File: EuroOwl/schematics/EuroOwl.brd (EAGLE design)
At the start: 100 x 99.8 mm, 122 parts, among them IC1 QUAD_OPAMPD, IC2 QUAD_OPAMPD, IC3 TL072D, Q900 BC846, Q901 BC846, X1 USBPTH-VERTICAL

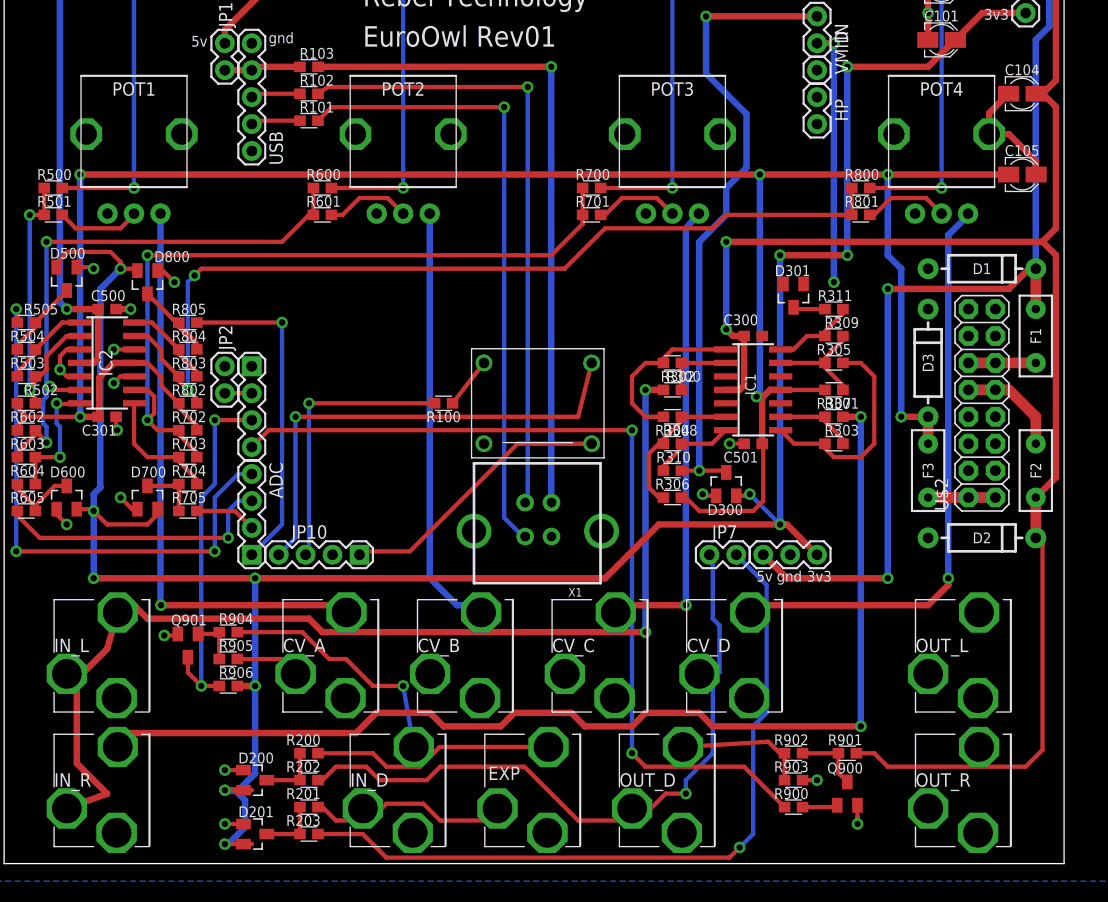
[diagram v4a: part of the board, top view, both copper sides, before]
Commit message: moved USB connector downwards
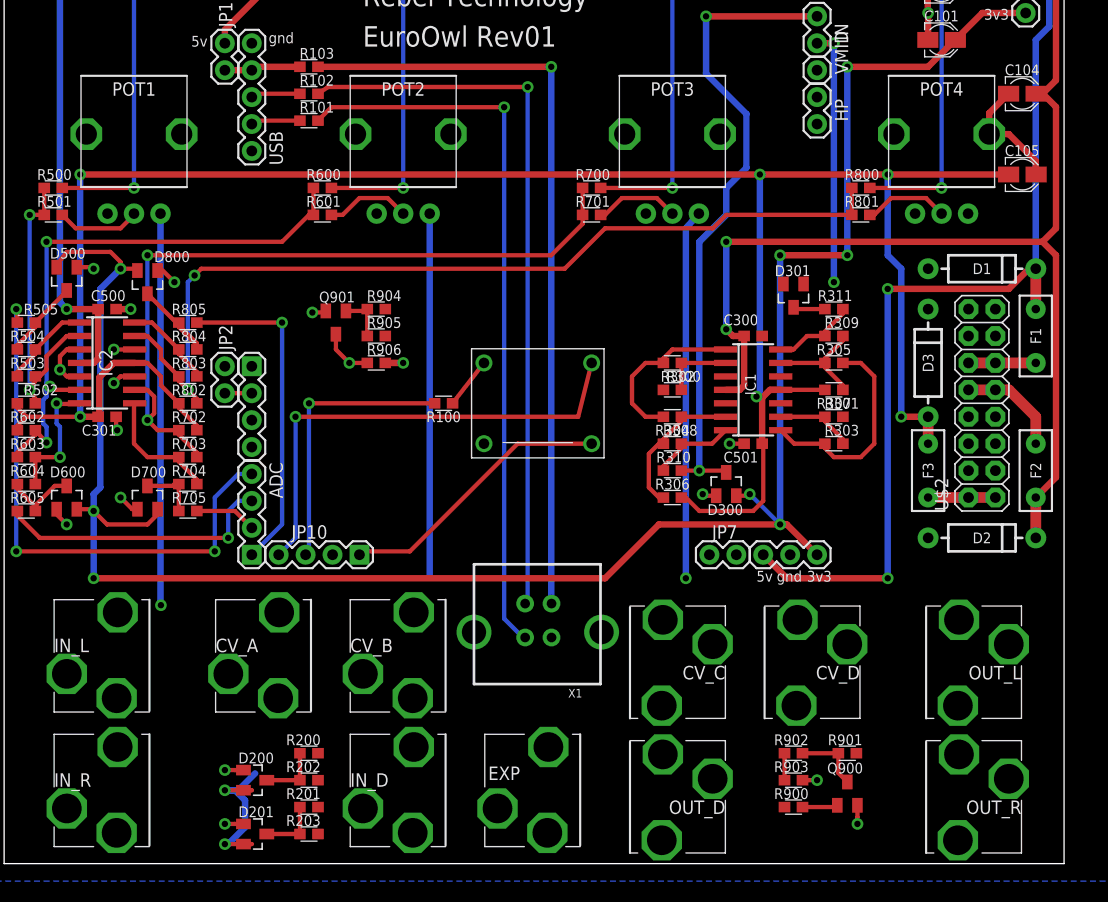
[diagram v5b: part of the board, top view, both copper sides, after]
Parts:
- moved R904 33.5 mm to (35.6, 53.3)
- moved Q901 33.5 mm to (31.8, 52.1)
- moved R905 33.5 mm to (35.6, 50.8)
- moved R906 33.5 mm to (35.6, 48.3)
- moved X1 9.52 mm to (50.8, 22.9)
- moved CV_D 6.35 mm to (76.2, 20.3), turned to 180 degrees
- moved CV_A 6.35 mm to (25.4, 20.3)
- moved CV_B 6.35 mm to (38.1, 20.3)
- moved CV_C 6.35 mm to (63.5, 20.3), turned to 180 degrees
- turned OUT_D to 180 degrees
- turned OUT_L to 180 degrees
- turned OUT_R to 180 degrees
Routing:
- net IN_R: track 106.0 -> 0.00 mm, vias 2 -> 0
- net IN_L: track 99.1 -> 0.00 mm, vias 2 -> 0
- net PB6: track 83.5 -> 0.00 mm, vias 2 -> 0
- net PA3: track 71.0 -> 0.00 mm, vias 1 -> 0
- net PA2: track 63.7 -> 0.00 mm, vias 1 -> 0
- net N$30: track 57.2 -> 0.00 mm, vias 1 -> 0
- net +12V: track 294.3 -> 255.3 mm
- net PB7: track 34.0 -> 4.93 mm, vias 2 -> 1
- net N$46: track 23.6 -> 0.00 mm, vias 1 -> 0
- net N$38: track 23.0 -> 0.00 mm
- net N$47: track 19.3 -> 0.00 mm
- net +3V3: track 231.9 -> 213.5 mm, vias 12 -> 11
- net N$2: track 54.7 -> 37.0 mm
- net N$24: track 45.9 -> 34.9 mm
- net N$49: track 12.6 -> 2.54 mm
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
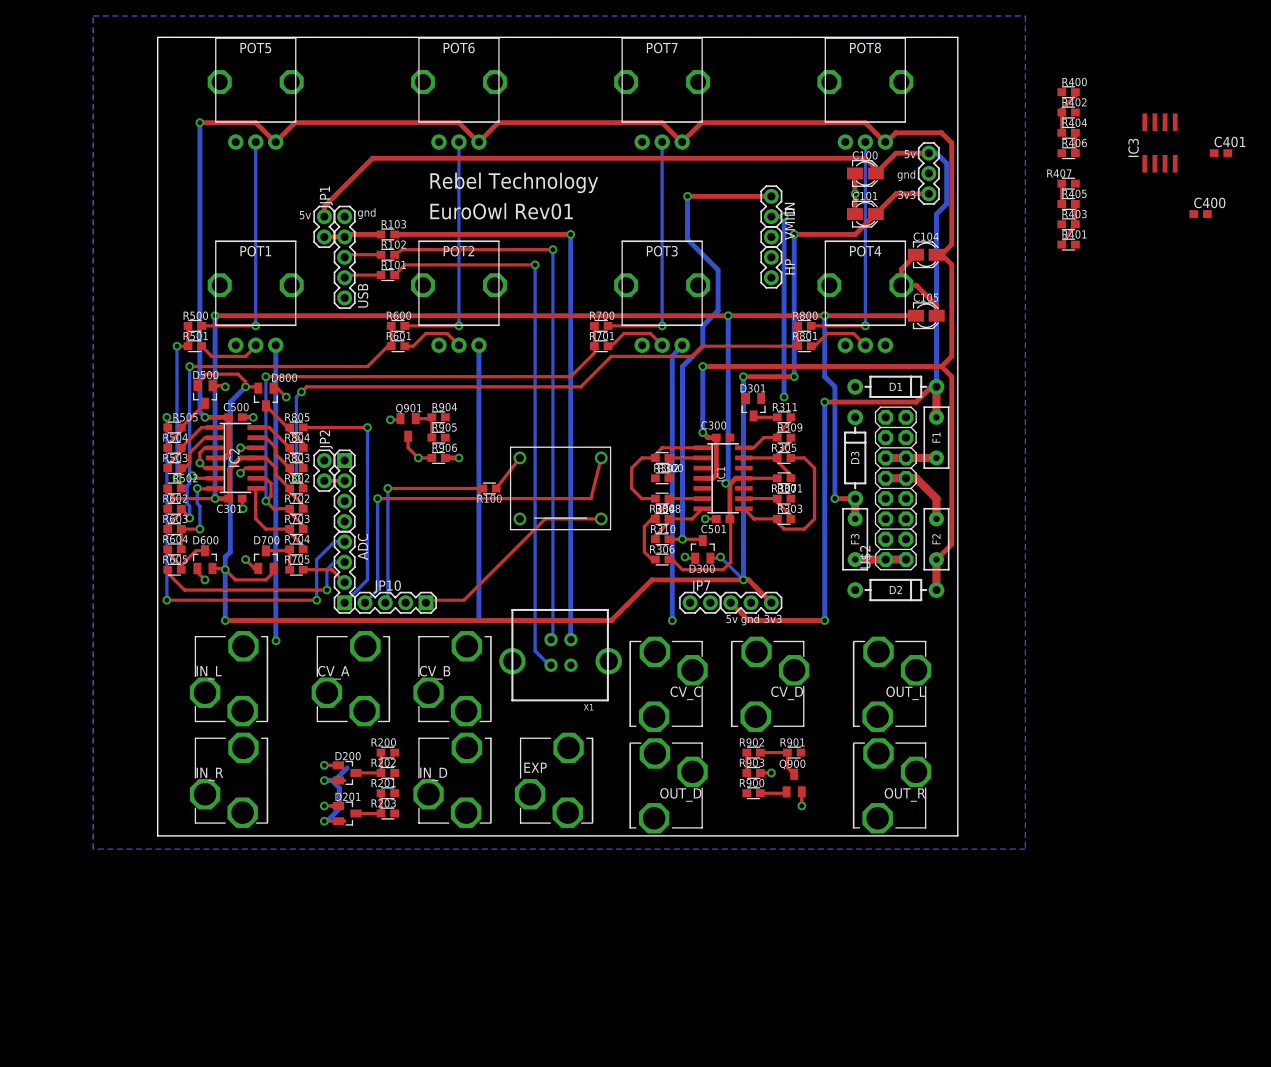
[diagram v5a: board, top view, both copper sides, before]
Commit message: added vdd pin to BOOT0 header to enable DFU mode
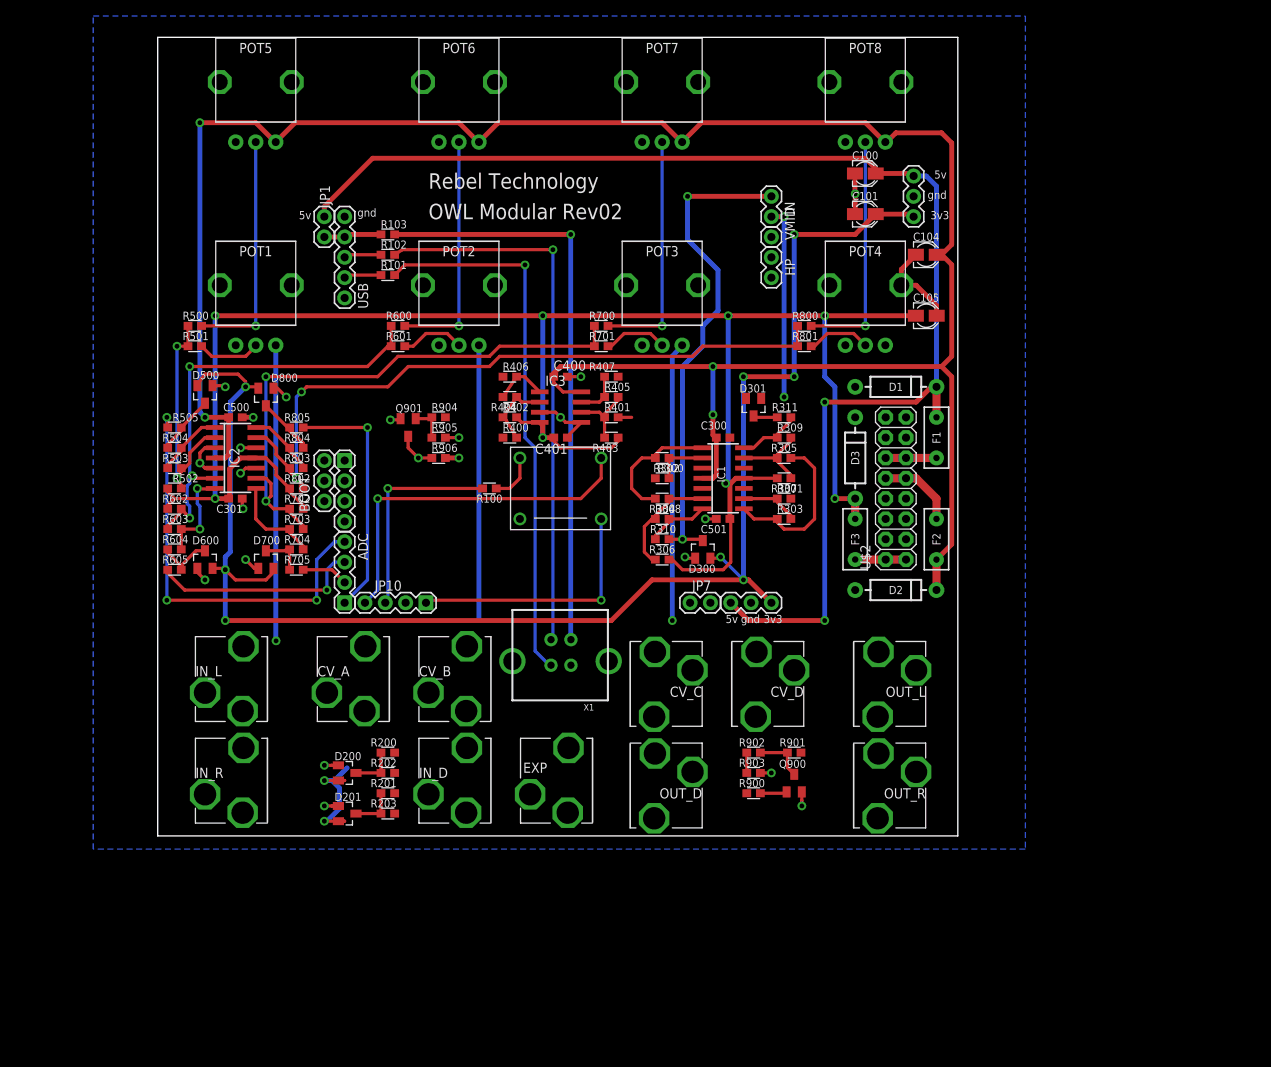
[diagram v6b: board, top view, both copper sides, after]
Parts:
- removed JP2: (no value), SparkFun:1X02
- added BOOT: (no value), SparkFun:1X03
- moved C401 89.9 mm to (50.8, 50.8), turned to 180 degrees
- moved C400 82.5 mm to (50.8, 58.4)
- moved R400 82.1 mm to (44.5, 50.8)
- moved IC3 81.9 mm to (50.8, 54.6), turned to 270 degrees
- moved R402 79.6 mm to (44.5, 53.3)
- moved R404 77.3 mm to (44.5, 55.9), turned to 180 degrees
- moved R406 75.2 mm to (44.5, 58.4)
- moved R403 63.1 mm to (57.1, 50.8), turned to 180 degrees
- moved R405 62.0 mm to (57.1, 55.9)
- moved R407 62.0 mm to (57.1, 58.4)
- moved R401 61.1 mm to (57.1, 53.3)
- moved JP4 3.43 mm to (94.9, 83.5)
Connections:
- net +3V3: now also BOOT.3
- net BOOT0: now also BOOT.2; no longer JP2.2
- net GND: now also BOOT.1; no longer JP2.1
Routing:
- net -12V: track 211.8 -> 243.3 mm, vias 6 -> 8
- net +12V: track 255.3 -> 278.2 mm
- net GND: track 47.6 -> 59.4 mm, vias 17 -> 20
- net PE5: track 26.2 -> 32.2 mm, vias 0 -> 1
- net +5V: track 171.5 -> 166.0 mm
- net N$39: track 2.54 -> 6.75 mm
- net N$41: track 5.78 -> 9.29 mm
- net N$42: track 5.60 -> 8.95 mm
- net N$40: track 2.54 -> 5.70 mm
- net +3V3: track 213.5 -> 210.7 mm
- net BOOT0: track 2.54 -> 0.00 mm
- net R_OUT: track 0.00 -> 1.69 mm
- net N$10: track 4.82 -> 6.03 mm
- net N$51: track 69.1 -> 68.3 mm
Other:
- board text added: "OWL Modular Rev02"
- board text removed: "EuroOwl Rev01"

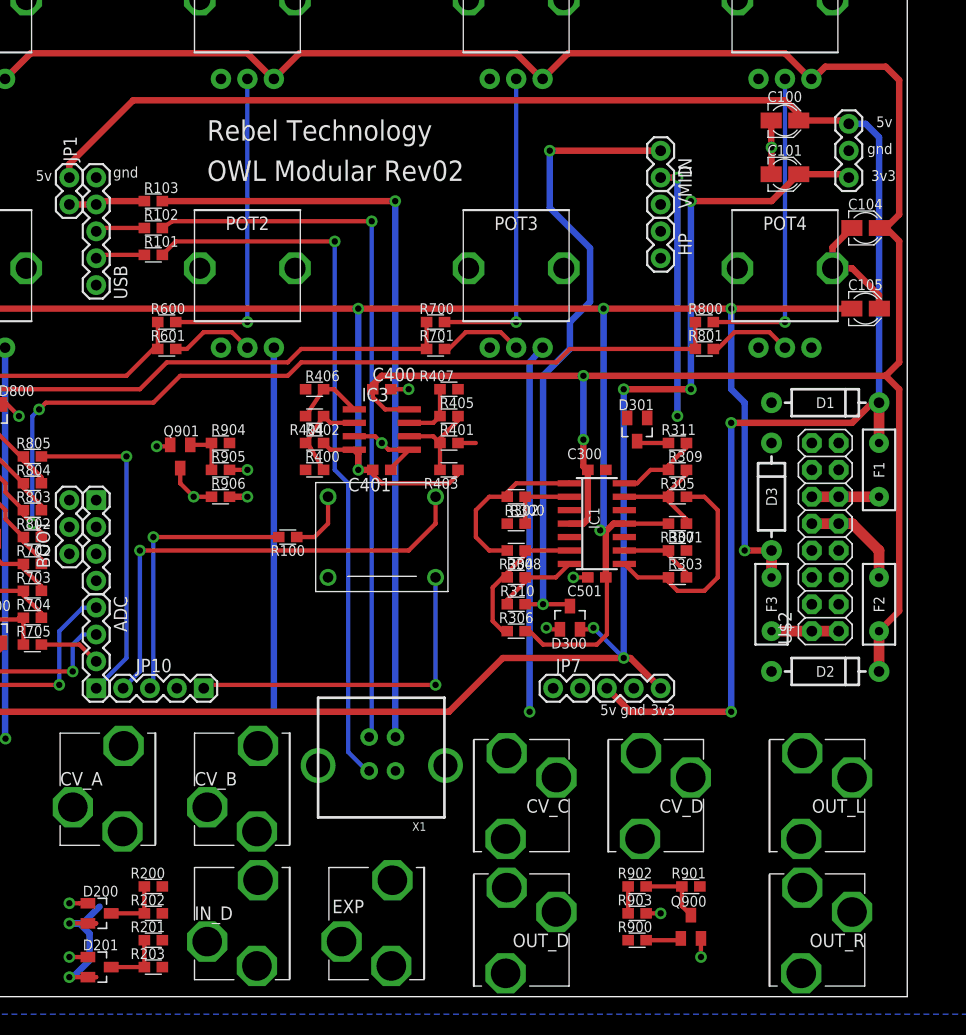
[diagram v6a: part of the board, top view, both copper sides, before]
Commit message: removed expression pedal ring, changed to mono input to PA2, normalled to GND
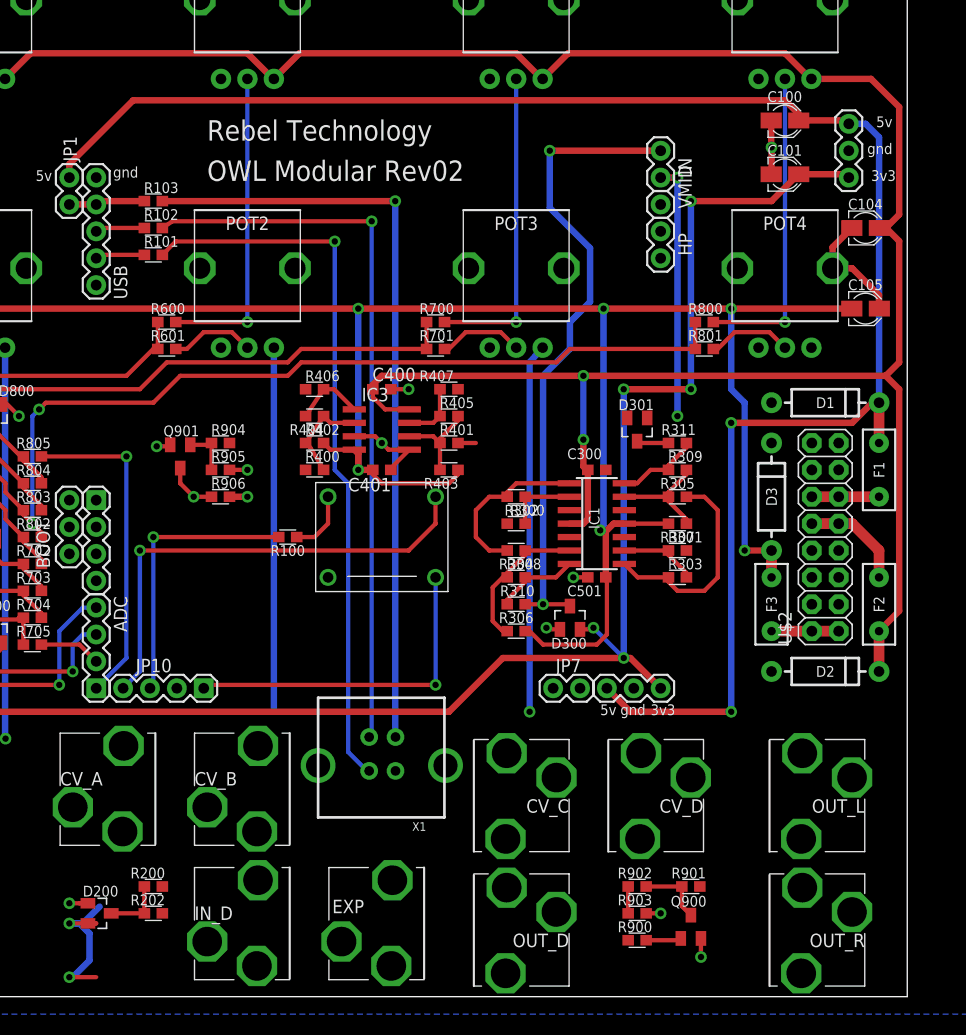
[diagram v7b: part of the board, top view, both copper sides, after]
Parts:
- removed D201: BAT54S, diode:SOT23
- removed R201, R203: 100R, Rebel:0603
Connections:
- removed net N$15: D201.3, R201.2, R203.1
- removed net N$47: EXP.P$1, R201.1
- net +3V3: no longer D201.2
- net GND: now also EXP.P$1; no longer D201.1
- net PA3: no longer R203.2
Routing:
- net N$15: track 5.67 -> 0.00 mm
- net +12V: track 278.2 -> 275.8 mm
- net GND: track 59.4 -> 57.6 mm, vias 20 -> 19
- net +3V3: track 210.7 -> 209.9 mm
